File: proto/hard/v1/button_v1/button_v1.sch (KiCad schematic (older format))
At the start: 37 parts, among them J10 Conn_01x05_Male, J14 K3-2235D, J7 Conn_01x04_Female, J9 Conn_01x06_Male, Q1 TP0610T, Q3 TP0610T, Q8 IRLML2803, U1 LCD_2.8_SPI, U11 TC305, U12 LCD_1_8_SPI, U2 STM32F103C8Tx, Y1 8MHz

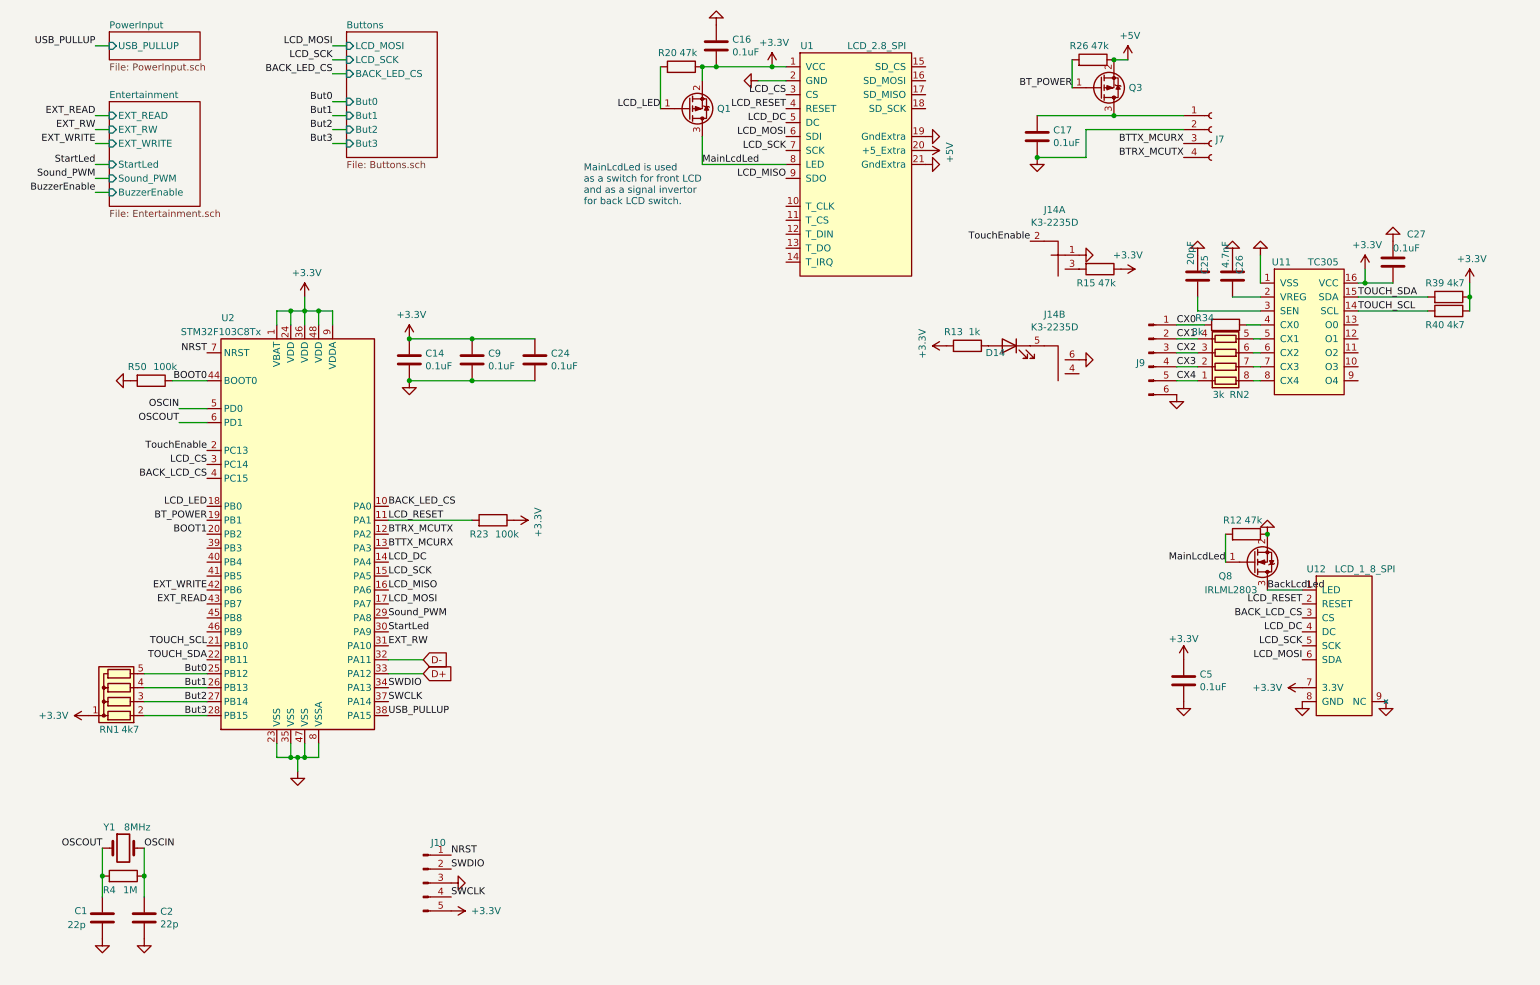
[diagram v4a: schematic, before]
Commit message: Rework of main board prototype. Work not finished.
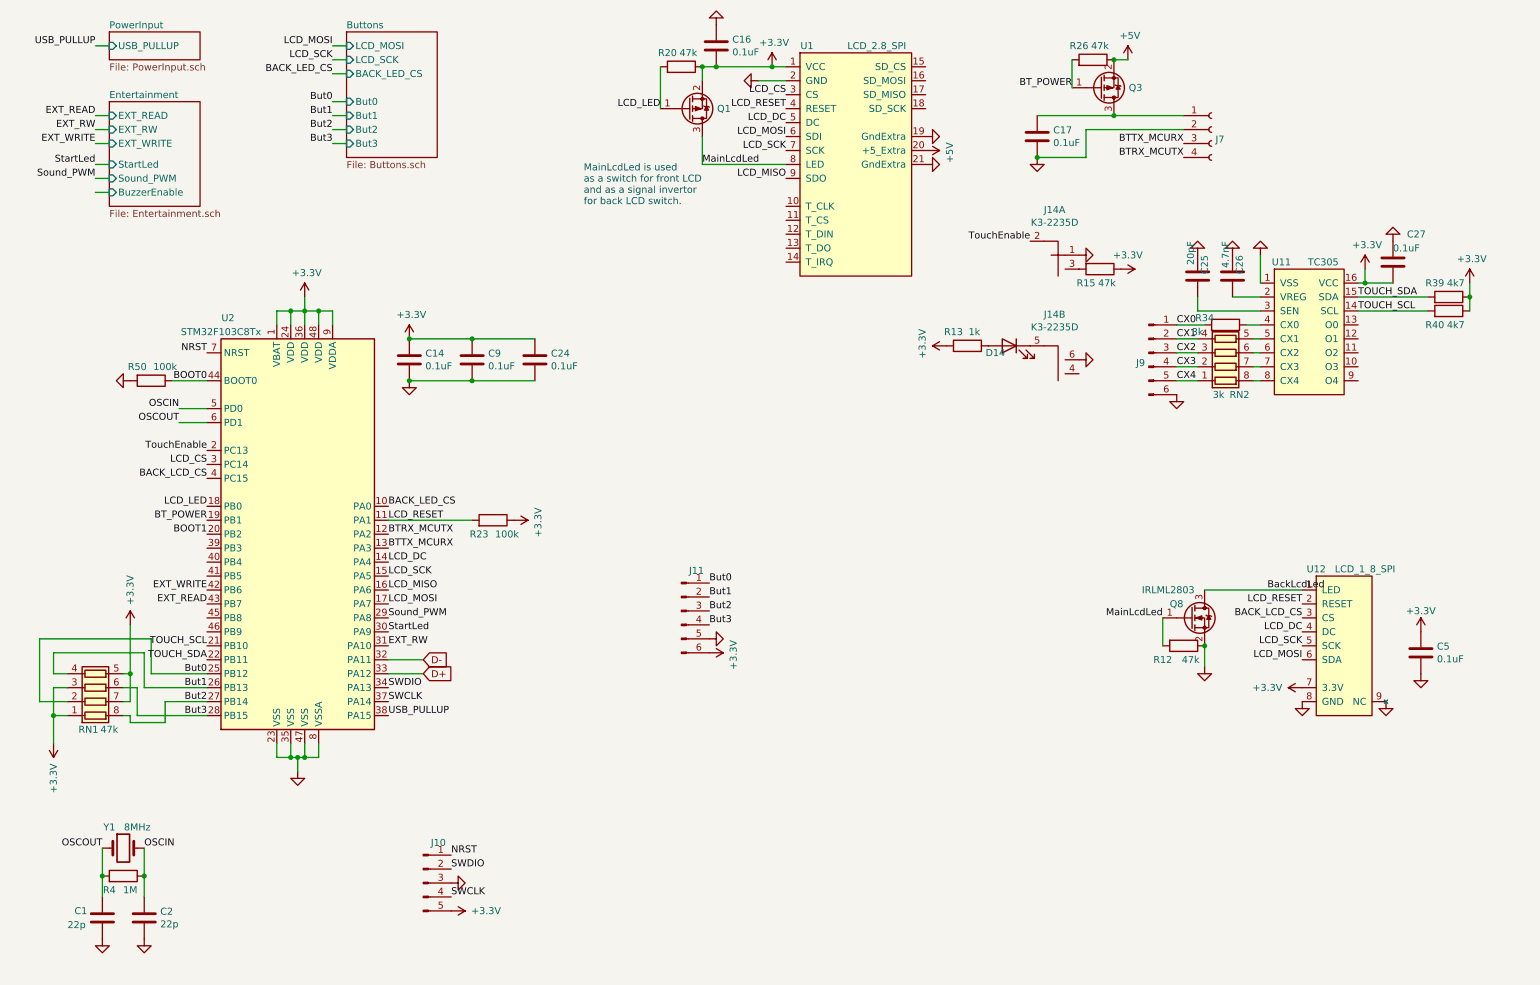
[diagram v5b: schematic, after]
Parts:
- removed RN1: 4k7, Resistor_THT:R_Array_SIP5, symbol Device:R_Network04
- added J11: Conn_01x06_Male, brbuttonsystem:JST_ZH_B6B-ZR_1x06_P1.50mm_Vertical, symbol Connector:Conn_01x06_Male
- added RN1: 47k, Resistor_SMD:R_Array_Convex_4x0603, symbol Device:R_Pack04
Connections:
- net +3V3: now also J11.6 (Pin_6), RN1.1 (R1.1), RN1.3 (R3.1), RN1.5 (R4.2), RN1.7 (R2.2)
- net But0: now also J11.1 (Pin_1), RN1.2 (R2.1)
- net But1: now also J11.2 (Pin_2), RN1.4 (R4.1)
- net But2: now also J11.3 (Pin_3), RN1.8 (R1.2)
- net But3: now also J11.4 (Pin_4), RN1.6 (R3.2)
- net GND: now also J11.5 (Pin_5)
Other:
- moved on the sheet: C5, Q8, R12
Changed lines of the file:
@@
 Text Label 3150 4800 0    50   ~ 0
 LCD_MOSI
-$Comp
-L power:+3.3V #PWR030
-U 1 1 5CFE0A9B
-P 1000 5600
-F 0 "#PWR030" H 1000 5450 50  0001 C CNN
-F 1 "+3.3V" V 1000 5850 50  0000 C CNN
-F 2 "" H 1000 5600 50  0001 C CNN
-F 3 "" H 1000 5600 50  0001 C CNN
-	1    1000 5600
-	0    -1   -1   0
-$EndComp
 Text Label 1850 5600 2    50   ~ 0
 But3
@@
 Text Label 3150 4100 0    50   ~ 0
 BACK_LED_CS
-Text Label 1050 1850 2    50   ~ 0
-BuzzerEnable
 Wire Wire Line
 	1050 1850 1150 1850
@@
 	1    0    0    -1
 $EndComp
-$Comp
-L Device:R_Network04 RN1
-U 1 1 5D925F5A
-P 1200 5400
-F 0 "RN1" V 900 5450 50  0000 C CNN
-F 1 "4k7" V 900 5300 50  0000 C CNN
-F 2 "Resistor_THT:R_Array_SIP5" V 1475 5400 50  0001 C CNN
-F 3 "http://www.vishay.com/docs/31509/csc.pdf" H 1200 5400 50  0001 C CNN
-	1    1200 5400
-	0    -1   -1   0
-$EndComp
-Wire Wire Line
-	1850 5600 1400 5600
-Wire Wire Line
-	1400 5500 1850 5500
-Wire Wire Line
-	1850 5400 1400 5400
-Wire Wire Line
-	1400 5300 1850 5300
+Wire Wire Line
+	1450 5300 1850 5300
 $Comp
 L brbuttonsystem:LCD_1_8_SPI U12
@@
 L Transistor_FET:IRLML2060 Q8
 U 1 1 5D68AB43
-P 9350 4500
-F 0 "Q8" H 9100 4600 50  0000 L CNN
-F 1 "IRLML2803" H 9000 4700 50  0000 L CNN
-F 2 "Package_TO_SOT_SMD:SOT-23" H 9550 4425 50  0001 L CIN
-F 3 "https://www.infineon.com/dgdl/irlml2060pbf.pdf?fileId=5546d462533600a401535664b7fb25ee" H 9350 4500 50  0001 L CNN
-	1    9350 4500
-	1    0    0    1
-$EndComp
-Wire Wire Line
-	9700 4700 9450 4700
+P 8900 4900
+F 0 "Q8" H 8750 5000 50  0000 L CNN
+F 1 "IRLML2803" H 8550 5100 50  0000 L CNN
+F 2 "Package_TO_SOT_SMD:SOT-23" H 9100 4825 50  0001 L CIN
+F 3 "https://www.infineon.com/dgdl/irlml2060pbf.pdf?fileId=5546d462533600a401535664b7fb25ee" H 8900 4900 50  0001 L CNN
+	1    8900 4900
+	1    0    0    -1
+$EndComp
 $Comp
 L Device:R R20
@@
 L Device:R R12
 U 1 1 5D6CBE16
-P 9300 4300
-F 0 "R12" V 9400 4200 50  0000 C CNN
-F 1 "47k" V 9400 4350 50  0000 C CNN
-F 2 "Resistor_SMD:R_0805_2012Metric_Pad1.15x1.40mm_HandSolder" V 9230 4300 50  0001 C CNN
-F 3 "~" H 9300 4300 50  0001 C CNN
-	1    9300 4300
-	0    1    -1   0
-$EndComp
-Wire Wire Line
-	9150 4500 9150 4300
+P 8850 5100
+F 0 "R12" V 8950 4950 50  0000 C CNN
+F 1 "47k" V 8950 5150 50  0000 C CNN
+F 2 "Resistor_SMD:R_0805_2012Metric_Pad1.15x1.40mm_HandSolder" V 8780 5100 50  0001 C CNN
+F 3 "~" H 8850 5100 50  0001 C CNN
+	1    8850 5100
+	0    1    1    0
+$EndComp
+Wire Wire Line
+	8700 4900 8700 5100
 $Comp
 L power:GND #PWR0142
 U 1 1 5D6EB51B
-P 9450 4300
-F 0 "#PWR0142" H 9450 4050 50  0001 C CNN
-F 1 "GND" H 9455 4127 50  0001 C CNN
-F 2 "" H 9450 4300 50  0001 C CNN
-F 3 "" H 9450 4300 50  0001 C CNN
-	1    9450 4300
-	-1   0    0    1
-$EndComp
-Connection ~ 9450 4300
+P 9000 5250
+F 0 "#PWR0142" H 9000 5000 50  0001 C CNN
+F 1 "GND" H 9005 5077 50  0001 C CNN
+F 2 "" H 9000 5250 50  0001 C CNN
+F 3 "" H 9000 5250 50  0001 C CNN
+	1    9000 5250
+	-1   0    0    -1
+$EndComp
+Connection ~ 9000 5100
 Text Label 5400 1650 0    50   ~ 0
 MainLcdLed
@@
 Text Label 1850 3000 2    50   ~ 0
 NRST
-Text Label 9150 4500 2    50   ~ 0
+Text Label 8700 4900 2    50   ~ 0
 MainLcdLed
 $Comp
@@
 L Device:C C5
 U 1 1 5F20E3F6
-P 8850 5350
-F 0 "C5" H 8965 5396 50  0000 L CNN
-F 1 "0.1uF" H 8965 5305 50  0000 L CNN
-F 2 "Capacitor_SMD:C_0805_2012Metric_Pad1.15x1.40mm_HandSolder" H 8888 5200 50  0001 C CNN
-F 3 "~" H 8850 5350 50  0001 C CNN
-	1    8850 5350
+P 10550 5150
+F 0 "C5" H 10665 5196 50  0000 L CNN
+F 1 "0.1uF" H 10665 5105 50  0000 L CNN
+F 2 "Capacitor_SMD:C_0805_2012Metric_Pad1.15x1.40mm_HandSolder" H 10588 5000 50  0001 C CNN
+F 3 "~" H 10550 5150 50  0001 C CNN
+	1    10550 5150
 	1    0    0    -1
 $EndComp
@@
 L power:GND #PWR0170
 U 1 1 5F20F286
-P 8850 5500
-F 0 "#PWR0170" H 8850 5250 50  0001 C CNN
-F 1 "GND" H 8855 5327 50  0001 C CNN
-F 2 "" H 8850 5500 50  0001 C CNN
-F 3 "" H 8850 5500 50  0001 C CNN
-	1    8850 5500
+P 10550 5300
+F 0 "#PWR0170" H 10550 5050 50  0001 C CNN
+F 1 "GND" H 10555 5127 50  0001 C CNN
+F 2 "" H 10550 5300 50  0001 C CNN
+F 3 "" H 10550 5300 50  0001 C CNN
+	1    10550 5300
 	1    0    0    -1
 $EndComp
@@
 L power:+3.3V #PWR0171
 U 1 1 5F20F54B
-P 8850 5200
-F 0 "#PWR0171" H 8850 5050 50  0001 C CNN
-F 1 "+3.3V" H 8850 5350 50  0000 C CNN
-F 2 "" H 8850 5200 50  0001 C CNN
-F 3 "" H 8850 5200 50  0001 C CNN
-	1    8850 5200
-	1    0    0    -1
+P 10550 5000
+F 0 "#PWR0171" H 10550 4850 50  0001 C CNN
+F 1 "+3.3V" H 10550 5150 50  0000 C CNN
+F 2 "" H 10550 5000 50  0001 C CNN
+F 3 "" H 10550 5000 50  0001 C CNN
+	1    10550 5000
+	1    0    0    -1
+$EndComp
+Wire Wire Line
+	9000 4700 9700 4700
+Wire Wire Line
+	9000 5250 9000 5100
+$Comp
+L Device:R_Pack04 RN1
+U 1 1 603F1D07
+P 1050 5400
+F 0 "RN1" V 750 5350 50  0000 C CNN
+F 1 "47k" V 750 5500 50  0000 C CNN
+F 2 "Resistor_SMD:R_Array_Convex_4x0603" V 1325 5400 50  0001 C CNN
+F 3 "~" H 1050 5400 50  0001 C CNN
+	1    1050 5400
+	0    1    -1   0
+$EndComp
+$Comp
+L power:+3.3V #PWR0179
+U 1 1 6040BC1B
+P 1300 4950
+F 0 "#PWR0179" H 1300 4800 50  0001 C CNN
+F 1 "+3.3V" V 1300 5200 50  0000 C CNN
+F 2 "" H 1300 4950 50  0001 C CNN
+F 3 "" H 1300 4950 50  0001 C CNN
+	1    1300 4950
+	1    0    0    -1
+$EndComp
+Wire Wire Line
+	1400 5400 1400 5150
+Wire Wire Line
+	1400 5150 750  5150
+Wire Wire Line
+	750  5150 750  5300
+Wire Wire Line
+	750  5300 850  5300
+Wire Wire Line
+	1400 5400 1850 5400
+Wire Wire Line
+	1450 5300 1450 5050
+Wire Wire Line
+	1450 5050 650  5050
+$Comp
+L power:+3.3V #PWR030
+U 1 1 5CFE0A9B
+P 750 5800
+F 0 "#PWR030" H 750 5650 50  0001 C CNN
+F 1 "+3.3V" V 750 6050 50  0000 C CNN
+F 2 "" H 750 5800 50  0001 C CNN
+F 3 "" H 750 5800 50  0001 C CNN
+	1    750  5800
+	-1   0    0    1
+$EndComp
+Wire Wire Line
+	850  5500 650  5500
+Wire Wire Line
+	650  5050 650  5500
+Wire Wire Line
+	850  5400 750  5400
+Wire Wire Line
+	750  5400 750  5600
+Wire Wire Line
+	850  5600 750  5600
+Connection ~ 750  5600
+Wire Wire Line
+	750  5600 750  5800
+Wire Wire Line
+	1250 5400 1350 5400
+Wire Wire Line
+	1250 5500 1300 5500
+Wire Wire Line
+	1300 5500 1300 5300
+Wire Wire Line
+	1250 5300 1300 5300
+Connection ~ 1300 5300
+Wire Wire Line
+	1300 5300 1300 4950
+Wire Wire Line
+	1350 5600 1350 5400
+Wire Wire Line
+	1850 5600 1350 5600
+Wire Wire Line
+	1850 5500 1550 5500
+Wire Wire Line
+	1550 5500 1550 5650
+Wire Wire Line
+	1550 5650 1300 5650
+Wire Wire Line
+	1300 5650 1300 5600
+Wire Wire Line
+	1300 5600 1250 5600
+$Comp
+L Connector:Conn_01x06_Male J11
+U 1 1 6049F9DA
+P 5250 4850
+F 0 "J11" H 5358 5139 50  0000 C CNN
+F 1 "Conn_01x06_Male" H 5358 5140 50  0001 C CNN
+F 2 "brbuttonsystem:JST_ZH_B6B-ZR_1x06_P1.50mm_Vertical" H 5250 4850 50  0001 C CNN
+F 3 "~" H 5250 4850 50  0001 C CNN
+	1    5250 4850
+	1    0    0    -1
+$EndComp
+Text Label 5450 4650 0    50   ~ 0
+But0
+Text Label 5450 4750 0    50   ~ 0
+But1
+Text Label 5450 4850 0    50   ~ 0
+But2
+Text Label 5450 4950 0    50   ~ 0
+But3
+$Comp
+L power:+3.3V #PWR0180
+U 1 1 604A1AF3
+P 5450 5150
+F 0 "#PWR0180" H 5450 5000 50  0001 C CNN
+F 1 "+3.3V" H 5465 5323 50  0000 C CNN
+F 2 "" H 5450 5150 50  0001 C CNN
+F 3 "" H 5450 5150 50  0001 C CNN
+	1    5450 5150
+	0    1    1    0
+$EndComp
+$Comp
+L power:GND #PWR0181
+U 1 1 604A1FB6
+P 5450 5050
+F 0 "#PWR0181" H 5450 4800 50  0001 C CNN
+F 1 "GND" H 5455 4877 50  0001 C CNN
+F 2 "" H 5450 5050 50  0001 C CNN
+F 3 "" H 5450 5050 50  0001 C CNN
+	1    5450 5050
+	0    -1   -1   0
 $EndComp
 $EndSCHEMATC

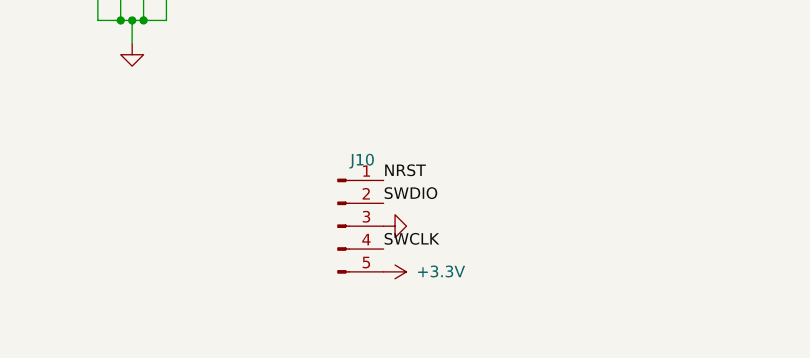
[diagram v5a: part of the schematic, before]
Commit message: Main PCB changes: - replaced flashing connected with 6-pin version. One of which should be removed. This is done to make flashing by not skilled pesons safer. Corresponding connector on programmer will have jammed hole. - moved connected for touch buttons lower. This should give more free space for wireless module connector.
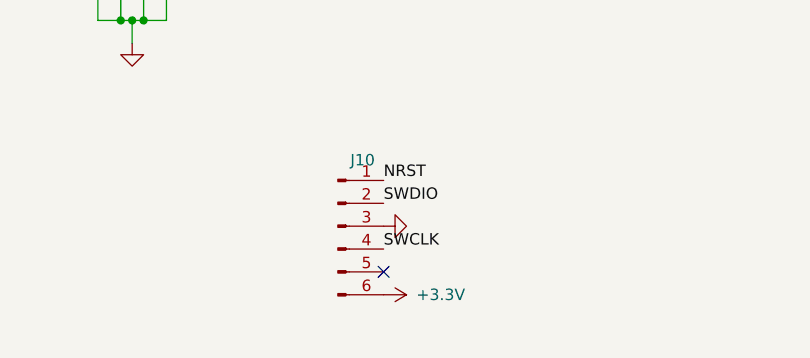
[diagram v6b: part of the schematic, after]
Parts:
- removed J10: Conn_01x05_Male, Connector_PinHeader_2.54mm:PinHeader_1x05_P2.54mm_Vertical, symbol Connector:Conn_01x05_Male
- added J10: Conn_01x06_Male, Connector_PinSocket_2.54mm:PinSocket_1x06_P2.54mm_Vertical, symbol Connector:Conn_01x06_Male
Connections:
- net +3V3: now also J10.6 (Pin_6)
- net GND: now also J10.3 (Pin_3)
- net NRST: now also J10.1 (Pin_1)
- net SWCLK: now also J10.4 (Pin_4)
- net SWDIO: now also J10.2 (Pin_2)
- no-connect marks 0 -> 1
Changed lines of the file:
@@
-$EndComp
-$Comp
-L Connector:Conn_01x05_Male J10
-U 1 1 5F1D58E0
-P 3400 6800
-F 0 "J10" H 3508 7089 50  0000 C CNN
-F 1 "Conn_01x05_Male" H 3508 7090 50  0001 C CNN
-F 2 "Connector_PinHeader_2.54mm:PinHeader_1x05_P2.54mm_Vertical" H 3400 6800 50  0001 C CNN
-F 3 "~" H 3400 6800 50  0001 C CNN
-	1    3400 6800
-	1    0    0    -1
 $EndComp
 $Comp
 L power:+3.3V #PWR0169
 U 1 1 5F1D7298
-P 3600 7000
-F 0 "#PWR0169" H 3600 6850 50  0001 C CNN
-F 1 "+3.3V" V 3600 7250 50  0000 C CNN
-F 2 "" H 3600 7000 50  0001 C CNN
-F 3 "" H 3600 7000 50  0001 C CNN
-	1    3600 7000
+P 3600 7100
+F 0 "#PWR0169" H 3600 6950 50  0001 C CNN
+F 1 "+3.3V" V 3600 7350 50  0000 C CNN
+F 2 "" H 3600 7100 50  0001 C CNN
+F 3 "" H 3600 7100 50  0001 C CNN
+	1    3600 7100
 	0    1    1    0
 $EndComp
@@
 	0    -1   -1   0
 $EndComp
+$Comp
+L Connector:Conn_01x06_Male J10
+U 1 1 607FBEF0
+P 3400 6800
+F 0 "J10" H 3508 7089 50  0000 C CNN
+F 1 "Conn_01x06_Male" H 3508 7090 50  0001 C CNN
+F 2 "Connector_PinSocket_2.54mm:PinSocket_1x06_P2.54mm_Vertical" H 3400 6800 50  0001 C CNN
+F 3 "~" H 3400 6800 50  0001 C CNN
+	1    3400 6800
+	1    0    0    -1
+$EndComp
+NoConn ~ 3600 7000
 $EndSCHEMATC
